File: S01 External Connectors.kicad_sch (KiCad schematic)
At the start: 43 parts, among them J1 1053101204, J2 1053101114, J3 10144517-043802LF, J4 1053102204, J5 1053091102, J6 1053091102, M1 78614150960, M2 78614150960, M3 78614150960, M4 78614150960, M5 78614150960, M6 78614150960

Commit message: Add a PCAL9714 SPI I/O expander for the load-switch enables and faults
New sheet S08 with U11 (PCAL9714, HVQFN-24) on the shared CLOCK/MOSI/MISO
bus. J3.32, which was ENSBC, becomes its chip select nCSIO.

- P0_0-P0_2 drive ENDAQ, ENSBC and ENEXT. J3.34/J3.36 become MCU_ENDAQ
  and MCU_ENEXT, and each reaches its enable only through a DNP 0R link
  (R96-R98). R95 links nCSIO to the expander CS.
- P0_4-P0_6 read the U6/U7/U9 power-good signals, and P0_7 reads U5
  nFLT/nINT.
- REGEN stays a direct J3.12 signal.
- RESET is divided from +12V (R99 100K, R100 40.2K), so the expander
  stays in reset while the 12 V rail is off.
- Pull-ups on CS and INT (R93, R94) and decoupling (C58, C59).

The README gains the port map, the links and the board work. The board
still needs Update PCB from Schematic.

Co-Authored-By: Claude Opus 5.5 <noreply@anthropic.com>
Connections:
- net ENDAQ renamed MCU_ENDAQ
- net ENEXT renamed MCU_ENEXT
- net ENSBC renamed nCSIO
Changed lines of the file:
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@@
 		)
 	)
-	(hierarchical_label "ENEXT"
+	(hierarchical_label "MCU_ENEXT"
 		(shape passive)
 		(at 248.92 162.56 0)
@@
 		)
 	)
-	(hierarchical_label "ENDAQ"
+	(hierarchical_label "MCU_ENDAQ"
 		(shape passive)
 		(at 248.92 158.75 0)
@@
 		)
 	)
-	(hierarchical_label "ENSBC"
+	(hierarchical_label "nCSIO"
 		(shape passive)
 		(at 248.92 154.94 0)

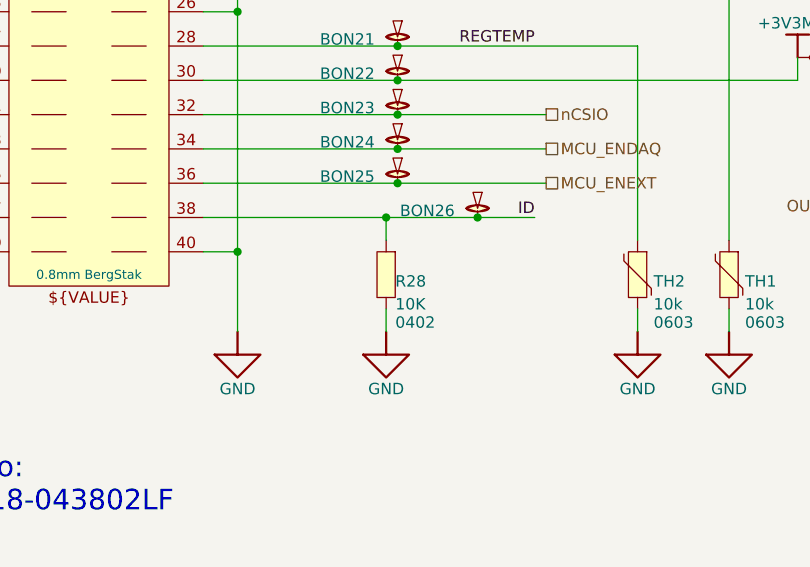
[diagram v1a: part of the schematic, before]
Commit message: Final-revision value changes and standard R/C symbols
Values (schematic and PCB):
- C2 100uF -> 82uF, matching the ordered 35SVPF82M
- C46, C47, C51 (TPS22811 DVDT) 4.7nF -> 1.8nF CC0402KRX7R9BB182 for a
  shorter output ramp
- R24-R27 10R -> 0R; D9, D10 and R36 DNP
- R14 0.01R -> 0.012R PA2512FKF7W0R012E

Symbols:
- All 160 resistors and capacitors now use Device:R, Device:C and
  Device:C_Polarized; the 76 per-value R/C symbols are removed from the
  project library. Connectivity is unchanged (netlist compared).
- Value is now the displayed field instead of ALTIUM_VALUE, which had left
  R1, C39 and R54 showing their old values. ALTIUM_VALUE synced with Value
  on R1, C39, R54, D1, Q1, Q3 and L1.
- Net-(C40-+) is now Net-(U5-ISNSP); renamed on the PCB and in the
  PWR 15A net class pattern.

Co-Authored-By: Claude Opus 5.5 <noreply@anthropic.com>
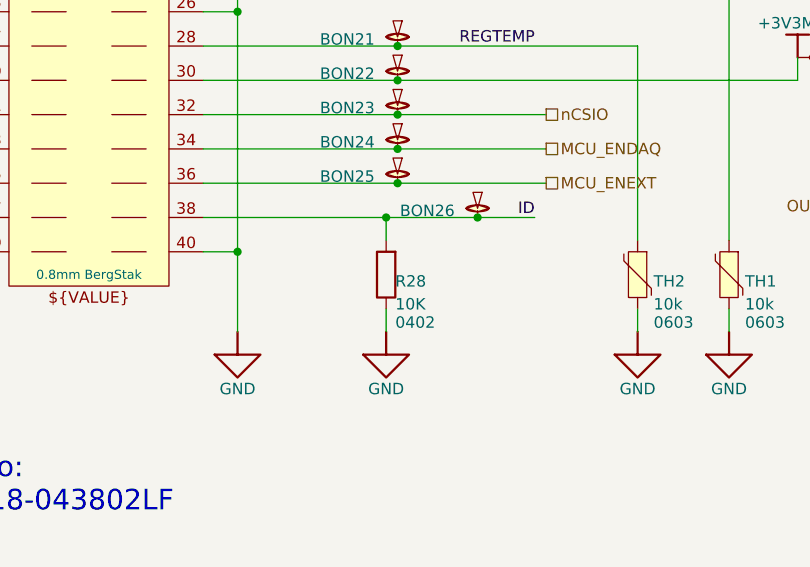
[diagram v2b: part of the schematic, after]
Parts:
- R28: symbol Lattech Systems:Resistor 10K 1% 0402 -> Device:R
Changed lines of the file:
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@@
 	)
 	(symbol
-		(lib_id "Lattech Systems:Resistor 10K 1% 0402")
-		(at 231.14 172.72 90)
+		(lib_id "Device:R")
+		(at 231.14 172.72 180)
 		(unit 1)
 		(body_style 1)
@@
 		(dnp no)
 		(property "Reference" "R28"
-			(at 232.156 172.72 90)
+			(at 232.156 172.72 0)
 			(show_name no)
 			(do_not_autoplace no)
@@
 		)
 		(property "Value" "10K"
-			(at 230.124 168.402 90)
-			(hide yes)
+			(at 232.156 175.26 0)
 			(show_name no)
 			(do_not_autoplace no)
@@
 		)
 		(property "Footprint" "Resistor_SMD:R_0402_1005Metric"
-			(at 231.14 172.72 0)
+			(at 231.14 172.72 90)
 			(hide yes)
 			(show_name no)
@@
 		)
 		(property "Datasheet" ""
-			(at 231.14 172.72 0)
+			(at 231.14 172.72 90)
 			(hide yes)
 			(show_name no)
@@
 		)
 		(property "Description" "Resistor 10K 1% 0402"
-			(at 231.14 172.72 0)
+			(at 231.14 172.72 90)
 			(hide yes)
 			(show_name no)
@@
 		)
 		(property "NOTE" ""
-			(at 230.124 168.402 90)
+			(at 230.124 168.402 0)
 			(hide yes)
 			(show_name no)
@@
 		)
 		(property "PL_SORT_GROUP" "2.3"
-			(at 230.124 168.402 90)
+			(at 230.124 168.402 0)
 			(hide yes)
 			(show_name no)
@@
 		)
 		(property "MANUFACTURER" "?"
-			(at 230.124 168.402 90)
+			(at 230.124 168.402 0)
 			(hide yes)
 			(show_name no)
@@
 		)
 		(property "MANUFACTURER_PN" "?"
-			(at 230.124 168.402 90)
+			(at 230.124 168.402 0)
 			(hide yes)
 			(show_name no)
@@
 		)
 		(property "ALTIUM_VALUE" "10K"
-			(at 232.156 175.26 90)
+			(at 230.124 168.402 0)
+			(hide yes)
 			(show_name no)
 			(do_not_autoplace no)
@@
 		)
 		(property "ALTIUM_FOOTPRINT" "0402"
-			(at 232.156 177.292 90)
+			(at 232.156 177.292 0)
 			(show_name no)
 			(do_not_autoplace no)

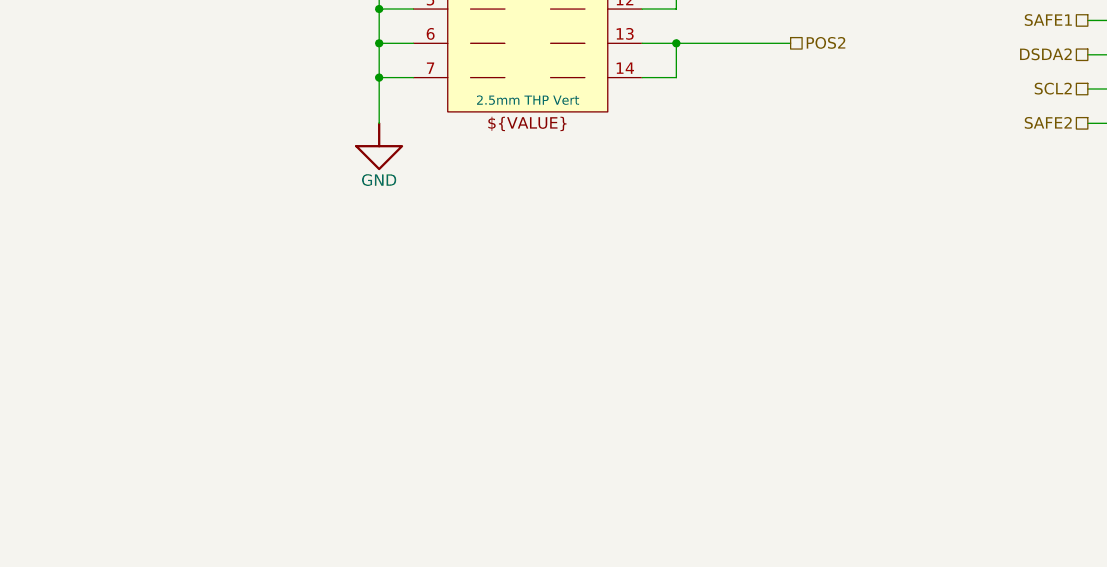
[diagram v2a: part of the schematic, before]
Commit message: Retune load-switch OVLO and PG dividers; add design constraint notes
- R90-R92 1M -> 1.07M: OVLO trips at 14.0 V (13.40-14.69 V) and recovers
  below 12.75 V (at least 12.23 V), so a tripped switch always comes back
  on the 12.03 V rail. R101 (Q23 gate divider) -> 1.07M to share the line.
- PGTH dividers R59/R61/R76 1M -> 100K and R60/R62/R77 130K -> 13K: same
  10.43 V threshold, but the +-1 uA pin leakage now moves it 0.1 V, not
  1 V; worst-case rising 10.93 V instead of 11.84 V.
- Schematic notes for the W16 constraints: J2 contacts (S01), R16 latching
  breaker and ED29/QE29 trip currents (S03), R19 vs L1 saturation (S04),
  R22 presence pull-up (S05), R42 and the U5 MODE/ILIMCOMP/VCC2 pins (S06),
  and the OVLO/PG divider settings (S07).
- README: OVLO and PG divider figures, and the EN_CONST_TDEAD default for
  the I2C build.

Co-Authored-By: Claude Opus 5.5 <noreply@anthropic.com>
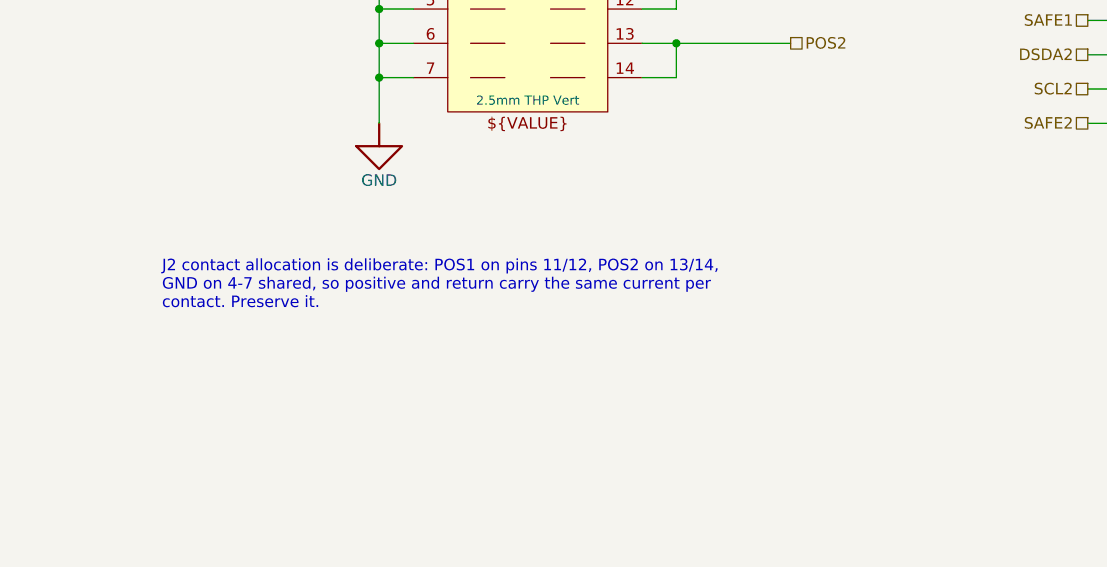
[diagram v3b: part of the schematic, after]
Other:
- note added: "J2 contact allocation is deliberate: POS1 on pins 11/12, POS2 on 13/14, GND on 4-7 shared, so positive and return carry the same current per contact. Preserve it."
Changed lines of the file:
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@@
 	(generator_version "10.0")
 	(paper "A3")
+	(text "J2 contact allocation is deliberate: POS1 on pins 11/12, POS2 on 13/14,\nGND on 4-7 shared, so positive and return carry the same current per\ncontact. Preserve it."
+		(exclude_from_sim no)
+		(at 44.45 181.61 0)
+		(effects
+			(font
+				(size 1.27 1.27)
+			)
+			(justify left top)
+		)
+	)
 	(text "9"
 		(exclude_from_sim no)

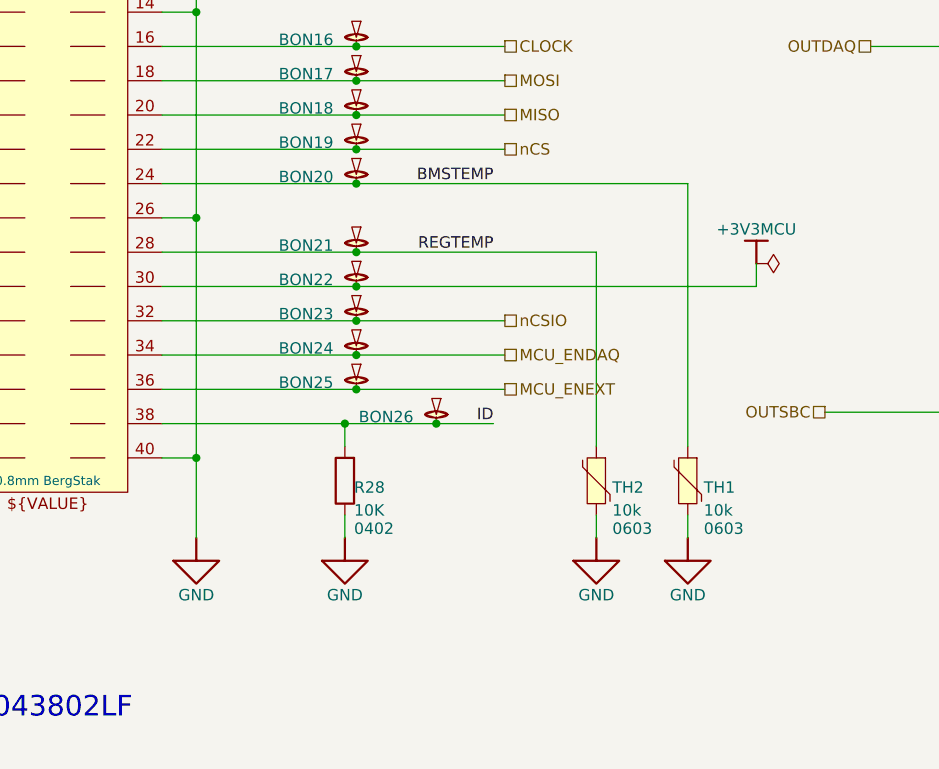
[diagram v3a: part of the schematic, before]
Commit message: PCB routing and DRC clean-up; teardrops; title block to 0.6.0
PCB (manual edits in KiCad):
- Route more of the new parts: +59 track segments, +7 vias, and a small
  +3V3MCU pour on In6.Cu near J3 (x 159, y 130-134).
- Add teardrops (319). Teardrop and zone defaults updated in the
  project settings.
- DRC with schematic parity: 285 -> 98 violations (64 padstack,
  27 unrouted pads, 19 + 2 silk, 8 text thickness, 5 dangling vias).
  No parity, clearance, short or courtyard errors.

Project: title-block variables BOARD_NUMBER EVO2513-0.6.0 and
COMP_NAME evoSonic; extra track width (0.15/0.5 mm) presets.

Schematics: cosmetic only (field positions, element order, S03 FET
pin entries). No value, footprint, DNP, net or note changes.

Molex 105310xx04 footprint: courtyard rectangle redrawn.

Co-Authored-By: Claude Opus 5.5 <noreply@anthropic.com>
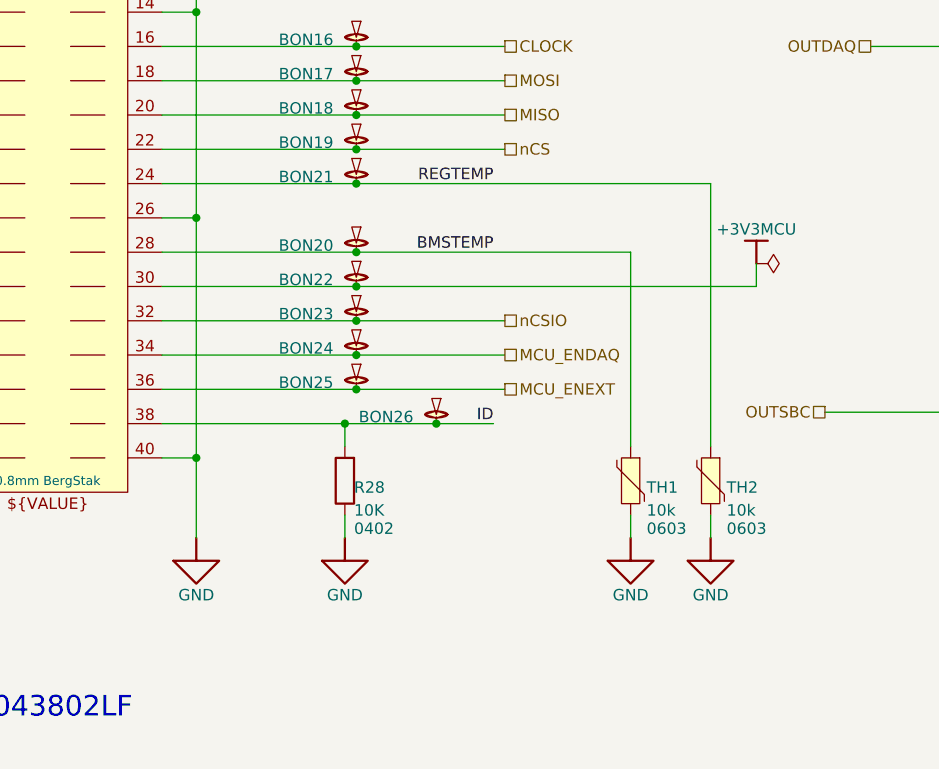
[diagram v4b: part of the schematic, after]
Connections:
- net BMSTEMP: now also J3.28 (I/O); no longer J3.24 (I/O)
- net REGTEMP: now also J3.24 (I/O); no longer J3.28 (I/O)
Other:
- moved on the sheet: BON20, BON21, TH1, TH2
